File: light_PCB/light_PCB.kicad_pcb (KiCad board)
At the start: 2 copper layers, 58 x 68 mm, 27 parts, among them J1 NUCLEO CONTROL, J2 12V POWER, J3 BLUE OUTPUT, J4 RED / NIR OUTPUT, J5 WHITE OUTPUT, Q1 AO3400A, Q2 AO3400A, Q3 AO3400A, Q4 AO3400A, Q5 AO3401A

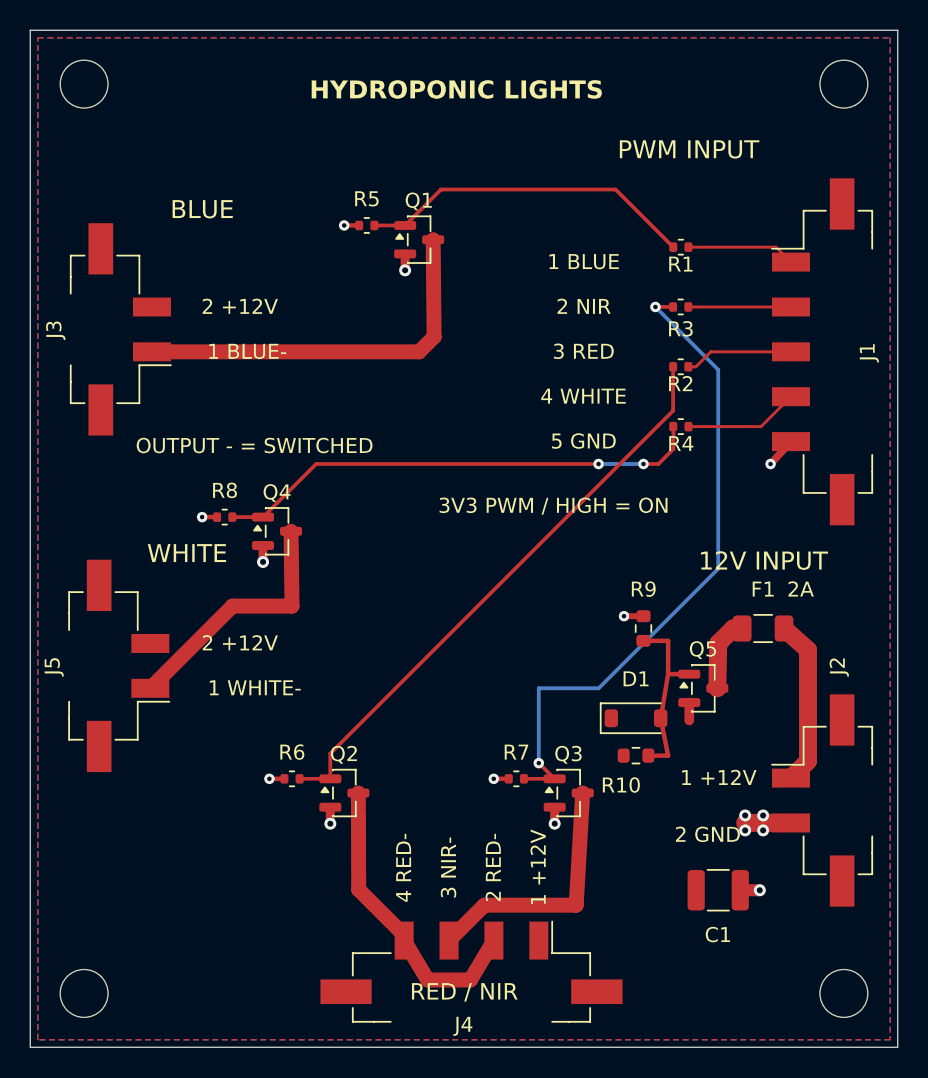
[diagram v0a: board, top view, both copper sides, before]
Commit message: Update four KiCad designs and include portable project libraries
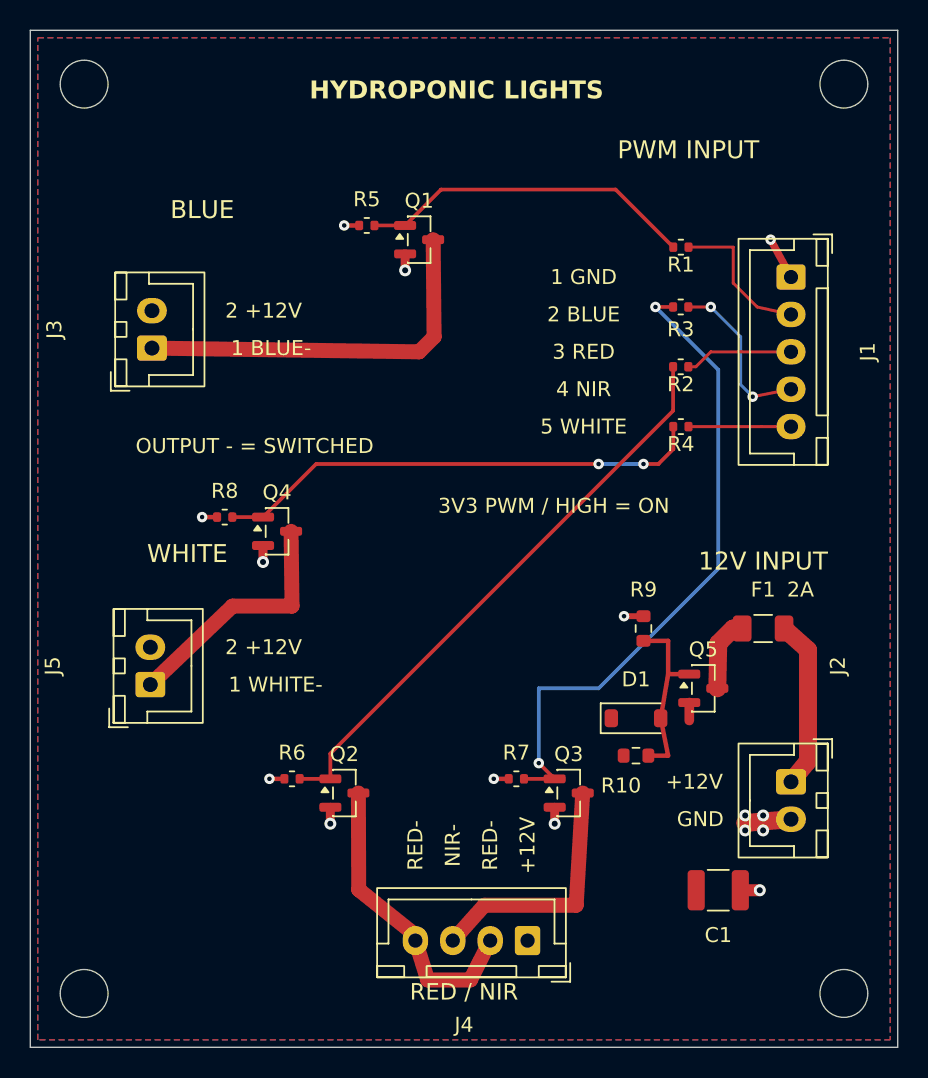
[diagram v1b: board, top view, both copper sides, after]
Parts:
- J1: value NUCLEO CONTROL -> BRAIN CONTROL; footprint Connector_Molex:Molex_Micro-Fit_3.0_43650-0524_1x05-1MP_P3.00mm_Vertical -> Connector_JST:JST_XH_B5B-XH-A_1x05_P2.50mm_Vertical
- J2, J3, J5: footprint Connector_Molex:Molex_Micro-Fit_3.0_43650-0224_1x02-1MP_P3.00mm_Vertical -> Connector_JST:JST_XH_B2B-XH-A_1x02_P2.50mm_Vertical
- J4: footprint Connector_Molex:Molex_Micro-Fit_3.0_43650-0424_1x04-1MP_P3.00mm_Vertical -> Connector_JST:JST_XH_B4B-XH-A_1x04_P2.50mm_Vertical
- moved J1 5.90 mm to (100.9, 59.5)
- moved J4 4.89 mm to (83.2, 103.9)
- moved J2 3.38 mm to (100.9, 93.2)
- moved J3 3.38 mm to (58.1, 64.2)
- moved J5 3.38 mm to (58.0, 86.8)
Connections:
- J1 pad 1: /BLUE_PWM -> /GND
- J1 pad 2: /NIR_PWM -> /BLUE_PWM
- J1 pad 4: /WHITE_PWM -> /NIR_PWM
- J1 pad 5: /GND -> /WHITE_PWM
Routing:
- net /NIR_PWM: track 6.86 -> 11.3 mm, vias 0 -> 2
- net /BLUE_PWM: track 7.28 -> 9.98 mm
- net /GND: track 18.1 -> 18.9 mm
- net /WHITE_PWM: track 7.68 -> 6.86 mm
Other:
- board text added: "+12V"
- board text added: "1 GND"
- board text added: "2 BLUE"
- board text added: "4 NIR"
- board text added: "5 WHITE"
- board text added: "GND"
- board text added: "NIR-"
- board text added: "RED-"
- board text removed: "1 +12V"
- board text removed: "1 BLUE"
- board text removed: "2 GND"
- board text removed: "2 NIR"
- board text removed: "2 RED-"
- board text removed: "3 NIR-"
- board text removed: "4 RED-"
- board text removed: "4 WHITE"
- board text removed: "5 GND"
